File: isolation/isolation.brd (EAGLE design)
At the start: 74.5 x 72.7 mm, 81 parts, among them IC1 XTLV61048DBVR, IC2 SN74HC14DRG3, IC3 SN74HCS32PWR, IC4 SN74HCS08DYYR, IC5 FDN359BN, IC6 FDN359BN, IC7 FDN359BN, IC8 FDN359BN, J1 S4B-PH-K-S(LF)(SN), J2 S4B-PH-K-S(LF)(SN), J3 S4B-PH-K-S(LF)(SN), J4 S4B-PH-K-S(LF)(SN), J5 S4B-PH-K-S(LF)(SN)

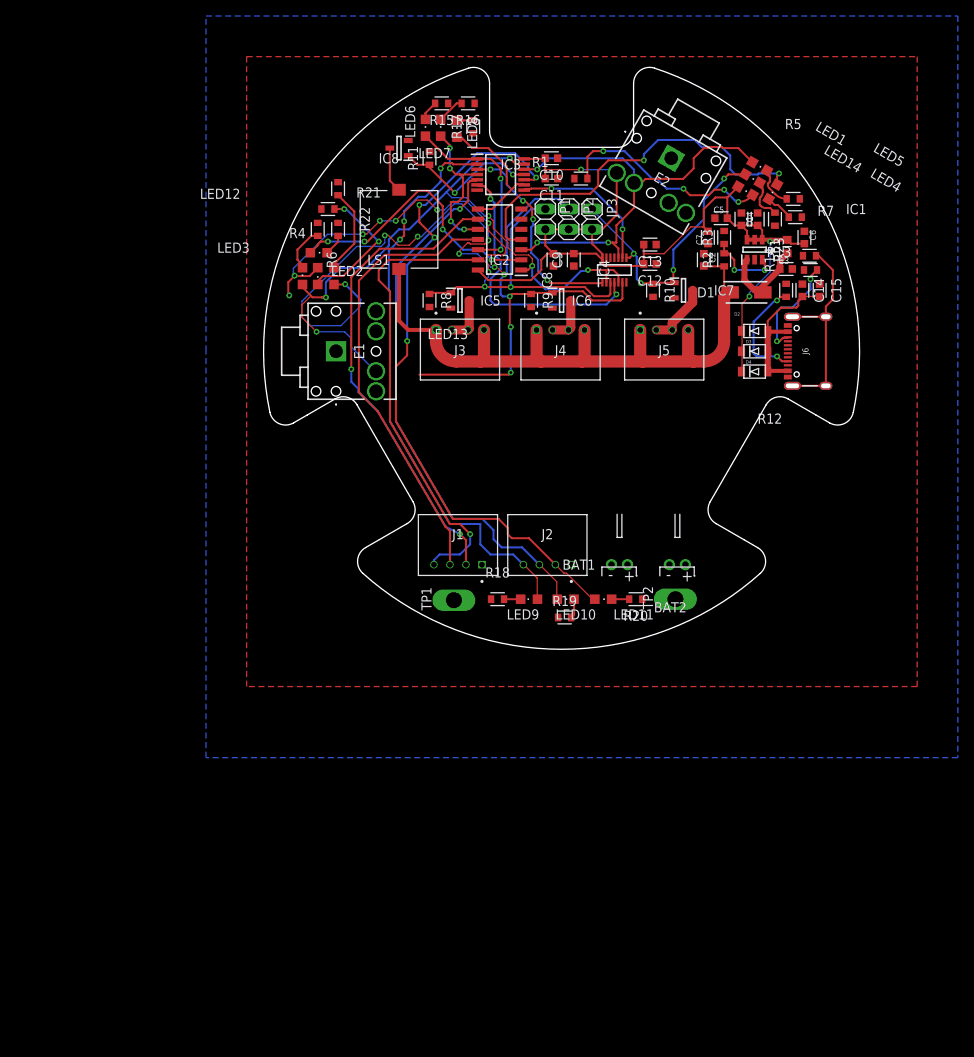
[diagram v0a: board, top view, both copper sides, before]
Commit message: 10mil dim line
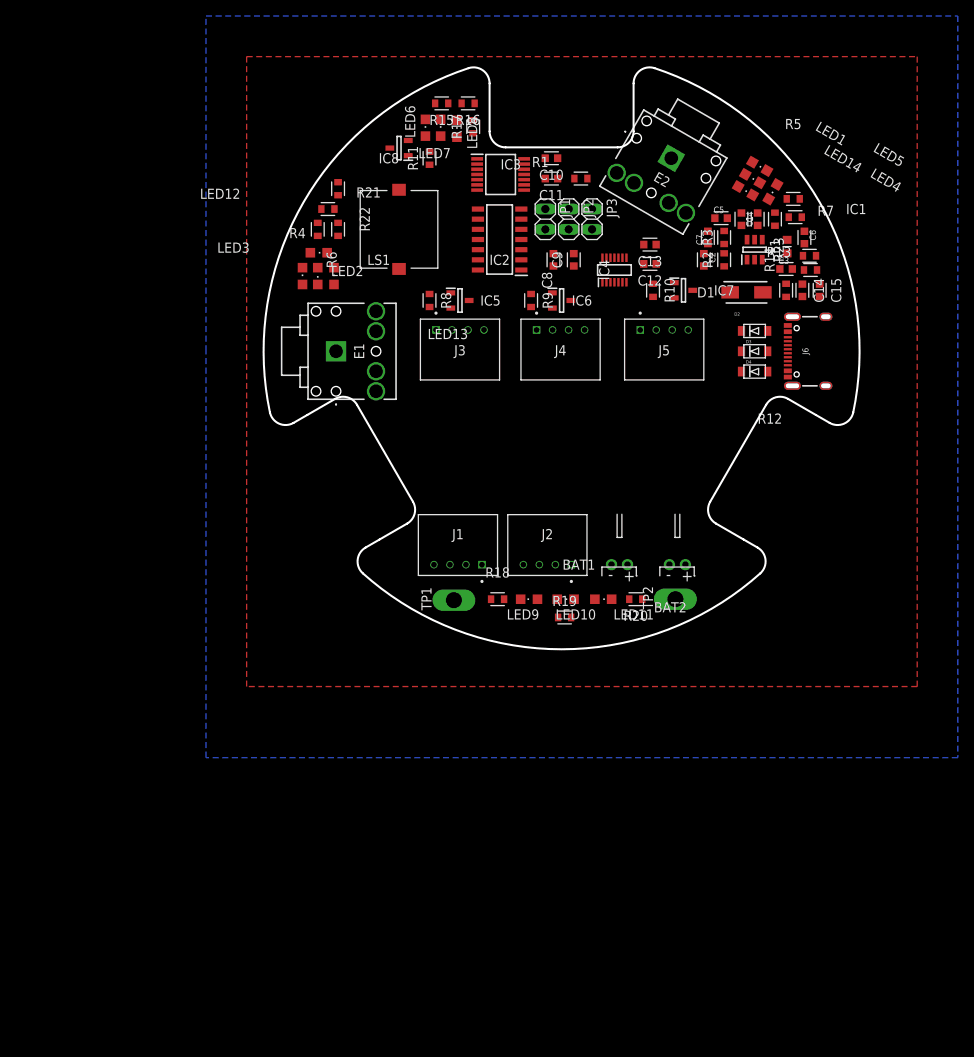
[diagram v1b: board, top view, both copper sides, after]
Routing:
- net VBAT: track 117.6 -> 0.00 mm, vias 3 -> 0
- net FIRE2: track 117.4 -> 0.00 mm, vias 10 -> 0
- net EN1: track 87.8 -> 0.00 mm, vias 6 -> 0
- net PICKLE3: track 86.7 -> 0.00 mm, vias 4 -> 0
- net FIRE1: track 86.2 -> 0.00 mm, vias 10 -> 0
- net VDEP: track 84.6 -> 0.00 mm
- net PICKLE1: track 72.8 -> 0.00 mm, vias 3 -> 0
- net PICKLE2: track 68.5 -> 0.00 mm, vias 1 -> 0
- net RAVEN3: track 59.9 -> 0.00 mm, vias 2 -> 0
- net EN2: track 57.7 -> 0.00 mm, vias 3 -> 0
- net RAVEN1: track 57.5 -> 0.00 mm, vias 1 -> 0
- net RAVEN2: track 56.1 -> 0.00 mm
- net SAFE2: track 49.2 -> 0.00 mm, vias 2 -> 0
- net FIRE3: track 36.1 -> 0.00 mm, vias 4 -> 0
- net SAFE1: track 34.9 -> 0.00 mm, vias 4 -> 0
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
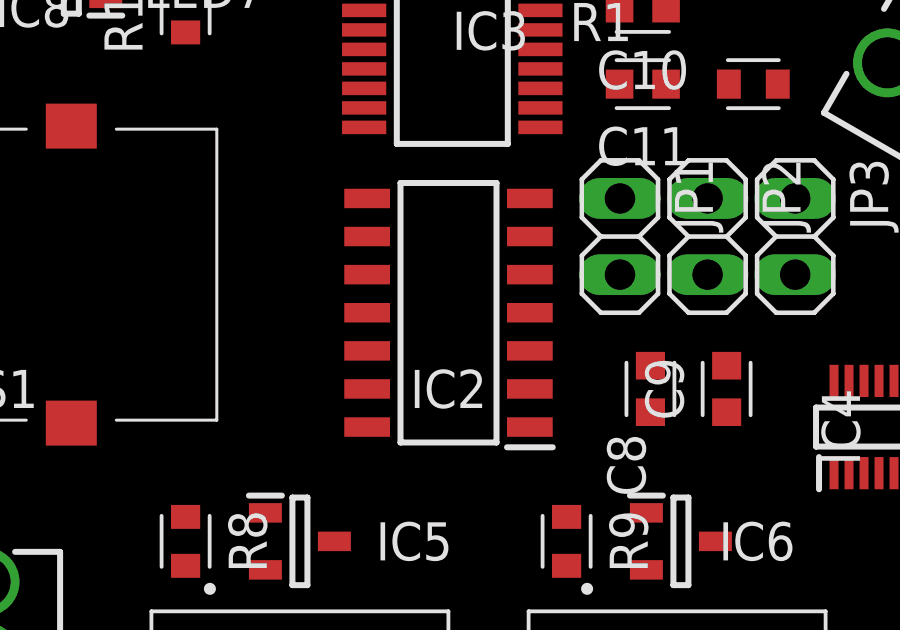
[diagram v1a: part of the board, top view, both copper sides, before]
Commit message: move to smaller inverter
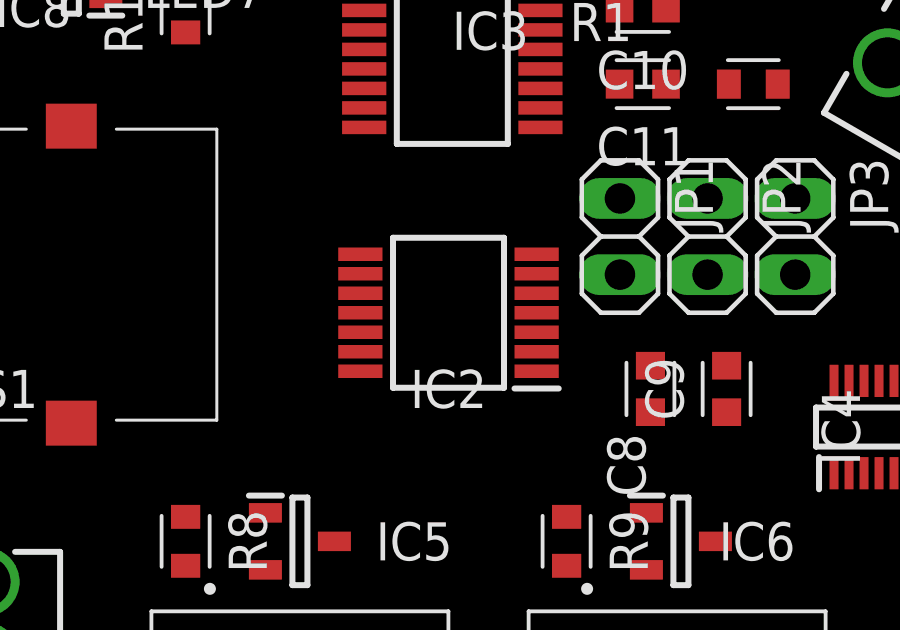
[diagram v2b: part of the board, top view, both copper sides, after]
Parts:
- IC2: value SN74HC14DRG3 -> SN74HC14PWR; device SamacSys_Parts:SOIC127P600X175-14N -> SamacSys_Parts:SOP65P640X120-14N
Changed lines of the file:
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@@
 <attribute name="VALUE" x="-27.844" y="0" size="1.27" layer="27" rot="R90" align="center"/>
 </element>
-<element name="IC2" library="SamacSys_Parts" package="SOIC127P600X175-14N" value="SN74HC14DRG3" x="-7.747" y="13.97" smashed="yes" rot="R180">
-<attribute name="ARROW_PART_NUMBER" value="SN74HC14DRG3" x="-7.747" y="13.97" size="1.778" layer="27" rot="R180" display="off"/>
-<attribute name="ARROW_PRICE-STOCK" value="https://www.arrow.com/en/products/sn74hc14drg3/texas-instruments?region=nac" x="-7.747" y="13.97" size="1.778" layer="27" rot="R180" display="off"/>
+<element name="IC2" library="SamacSys_Parts" package="SOP65P640X120-14N" value="SN74HC14PWR" x="-7.747" y="13.97" smashed="yes" rot="R180">
+<attribute name="ARROW_PART_NUMBER" value="SN74HC14PWR" x="-7.747" y="13.97" size="1.778" layer="27" rot="R180" display="off"/>
+<attribute name="ARROW_PRICE-STOCK" value="https://www.arrow.com/en/products/sn74hc14pwr/texas-instruments?region=nac" x="-7.747" y="13.97" size="1.778" layer="27" rot="R180" display="off"/>
 <attribute name="DESCRIPTION" value="Hex Schmitt-Trigger Inverters" x="-7.747" y="13.97" size="1.778" layer="27" rot="R180" display="off"/>
-<attribute name="HEIGHT" value="1.75mm" x="-7.747" y="13.97" size="1.778" layer="27" rot="R180" display="off"/>
+<attribute name="HEIGHT" value="1.2mm" x="-7.747" y="13.97" size="1.778" layer="27" rot="R180" display="off"/>
 <attribute name="MANUFACTURER_NAME" value="Texas Instruments" x="-7.747" y="13.97" size="1.778" layer="27" rot="R180" display="off"/>
-<attribute name="MANUFACTURER_PART_NUMBER" value="SN74HC14DRG3" x="-7.747" y="13.97" size="1.778" layer="27" rot="R180" display="off"/>
-<attribute name="MOUSER_PART_NUMBER" value="595-SN74HC14DRG3" x="-7.747" y="13.97" size="1.778" layer="27" rot="R180" display="off"/>
-<attribute name="MOUSER_PRICE-STOCK" value="https://www.mouser.co.uk/ProductDetail/Texas-Instruments/SN74HC14DRG3?qs=EuM%2FBx4ov4QCZjgspzZGxg%3D%3D" x="-7.747" y="13.97" size="1.778" layer="27" rot="R180" display="off"/>
+<attribute name="MANUFACTURER_PART_NUMBER" value="SN74HC14PWR" x="-7.747" y="13.97" size="1.778" layer="27" rot="R180" display="off"/>
+<attribute name="MOUSER_PART_NUMBER" value="595-SN74HC14PWR" x="-7.747" y="13.97" size="1.778" layer="27" rot="R180" display="off"/>
+<attribute name="MOUSER_PRICE-STOCK" value="https://www.mouser.co.uk/ProductDetail/Texas-Instruments/SN74HC14PWR?qs=YEaxc5757jODQ8PDizZzPA%3D%3D" x="-7.747" y="13.97" size="1.778" layer="27" rot="R180" display="off"/>
 <attribute name="NAME" x="-7.747" y="11.43" size="1.27" layer="25" rot="R180" align="center"/>
 <attribute name="VALUE" x="-7.747" y="13.97" size="1.27" layer="27" rot="R180" align="center"/>
@@
 <wire x1="-1.15" y1="5.4" x2="-1.016" y2="10.6554" width="0" layer="19" extent="1-1"/>
 <wire x1="-3.81" y1="5.5348" x2="-1.15" y2="5.4" width="0" layer="19" extent="1-1"/>
+<wire x1="-4.809" y1="14.62" x2="-1.016" y2="10.6554" width="0" layer="19" extent="1-1"/>
+<wire x1="-4.809" y1="15.92" x2="-4.809" y2="14.62" width="0" layer="19" extent="1-1"/>
 <wire x1="13.716" y1="24.13" x2="13.3810625" y2="18.549871875" width="0" layer="19" extent="1-1"/>
-<wire x1="-5.035" y1="15.24" x2="-1.016" y2="10.6554" width="0" layer="19" extent="1-1"/>
-<wire x1="-5.035" y1="17.78" x2="-5.035" y2="15.24" width="0" layer="19" extent="1-1"/>
-<wire x1="-0.4954" y1="21.59" x2="-5.035" y2="17.78" width="0" layer="19" extent="1-1"/>
+<wire x1="28.28" y1="-3.225" x2="28.28" y2="3.225" width="0" layer="19" extent="1-1"/>
+<wire x1="-0.4954" y1="21.59" x2="-4.809" y2="15.92" width="0" layer="19" extent="1-1"/>
 <wire x1="1.5978" y1="21.59" x2="-0.4954" y2="21.59" width="0" layer="19" extent="1-1"/>
 <wire x1="-0.4954" y1="24.13" x2="-0.4954" y2="21.59" width="0" layer="19" extent="1-1"/>
-<wire x1="-10.558" y1="20.148" x2="-5.035" y2="17.78" width="0" layer="19" extent="1-1"/>
-<wire x1="28.28" y1="-3.225" x2="28.28" y2="3.225" width="0" layer="19" extent="1-1"/>
+<wire x1="-10.558" y1="20.148" x2="-4.809" y2="15.92" width="0" layer="19" extent="1-1"/>
 <wire x1="-11.049" y1="27.2518" x2="-10.558" y2="20.148" width="0" layer="19" extent="1-1"/>
 <wire x1="-10.8688" y1="30.988" x2="-11.049" y2="27.2518" width="0" layer="19" extent="1-1"/>
@@
 <wire x1="-4.682" y1="24.048" x2="-2.0446" y2="24.13" width="0" layer="19" extent="1-1"/>
 <wire x1="6.885871875" y1="22.299871875" x2="3.81" y2="15.24" width="0" layer="19" extent="1-1"/>
-<wire x1="-10.459" y1="10.16" x2="-1.016" y2="12.2046" width="0" layer="19" extent="1-1"/>
+<wire x1="-10.685" y1="12.02" x2="-2.032" y2="15.24" width="0" layer="19" extent="1-1"/>
 <wire x1="22.4925" y1="2.54" x2="23.18" y2="13.95" width="0" layer="19" extent="1-1"/>
 <wire x1="22.4925" y1="0" x2="22.4925" y2="2.54" width="0" layer="19" extent="1-1"/>
 <wire x1="22.4925" y1="-2.54" x2="22.4925" y2="0" width="0" layer="19" extent="1-1"/>
-<wire x1="-23.194" y1="-5" x2="-10.459" y2="10.16" width="0" layer="19" extent="1-1"/>
+<wire x1="-23.194" y1="-5" x2="-10.685" y2="12.02" width="0" layer="19" extent="1-1"/>
 <wire x1="15.478" y1="-26.67" x2="22.4925" y2="-2.54" width="0" layer="19" extent="1-1"/>
 <wire x1="14.224" y1="-30.988" x2="15.478" y2="-26.67" width="0" layer="19" extent="1-1"/>
@@
 <contactref element="IC3" pad="13"/>
 <wire x1="-23.194" y1="-2.5" x2="-32.385" y2="8.348" width="0" layer="19" extent="1-1"/>
-<wire x1="-5.035" y1="10.16" x2="-23.194" y2="-2.5" width="0" layer="19" extent="1-1"/>
-<wire x1="5.604" y1="8.622" x2="-5.035" y2="10.16" width="0" layer="19" extent="1-1"/>
+<wire x1="-4.809" y1="12.02" x2="-23.194" y2="-2.5" width="0" layer="19" extent="1-1"/>
+<wire x1="5.604" y1="8.622" x2="-4.809" y2="12.02" width="0" layer="19" extent="1-1"/>
 <wire x1="7.104" y1="8.622" x2="5.604" y2="8.622" width="0" layer="19" extent="1-1"/>
-<wire x1="-4.682" y1="23.398" x2="-5.035" y2="10.16" width="0" layer="19" extent="1-1"/>
+<wire x1="-4.682" y1="23.398" x2="-4.809" y2="12.02" width="0" layer="19" extent="1-1"/>
 </signal>
 <signal name="N$5">
@@
 <contactref element="IC2" pad="2"/>
 <contactref element="LED3" pad="A"/>
-<wire x1="-5.035" y1="11.43" x2="-31.403" y2="12.319" width="0" layer="19" extent="1-1"/>
+<wire x1="-4.809" y1="12.67" x2="-31.403" y2="12.319" width="0" layer="19" extent="1-1"/>
 </signal>
 <signal name="EN2">
@@
 <wire x1="9.050934375" y1="21.049871875" x2="23.855671875" y2="23.639" width="0" layer="19" extent="1-1"/>
 <wire x1="7.104" y1="11.698" x2="9.050934375" y2="21.049871875" width="0" layer="19" extent="1-1"/>
-<wire x1="-5.035" y1="12.7" x2="7.104" y2="11.698" width="0" layer="19" extent="1-1"/>
-<wire x1="-4.682" y1="22.748" x2="-5.035" y2="12.7" width="0" layer="19" extent="1-1"/>
+<wire x1="-4.809" y1="13.32" x2="7.104" y2="11.698" width="0" layer="19" extent="1-1"/>
+<wire x1="-4.682" y1="22.748" x2="-4.809" y2="13.32" width="0" layer="19" extent="1-1"/>
 </signal>
 <signal name="SAFE2">
 <contactref element="IC2" pad="4"/>
 <contactref element="LED5" pad="A"/>
-<wire x1="-5.035" y1="13.97" x2="26.941" y2="20.848325" width="0" layer="19" extent="1-1"/>
+<wire x1="-4.809" y1="13.97" x2="26.941" y2="20.848325" width="0" layer="19" extent="1-1"/>
 </signal>
 <signal name="N$6">
@@
 <contactref element="J1" pad="2"/>
 <contactref element="IC2" pad="9"/>
-<wire x1="-10.459" y1="16.51" x2="-11.954" y2="-26.67" width="0" layer="19" extent="1-1"/>
+<wire x1="-10.685" y1="15.27" x2="-11.954" y2="-26.67" width="0" layer="19" extent="1-1"/>
 </signal>
 <signal name="RAVEN2">
 <contactref element="J1" pad="3"/>
 <contactref element="IC2" pad="11"/>
-<wire x1="-10.459" y1="13.97" x2="-13.954" y2="-26.67" width="0" layer="19" extent="1-1"/>
+<wire x1="-10.685" y1="13.97" x2="-13.954" y2="-26.67" width="0" layer="19" extent="1-1"/>
 </signal>
 <signal name="RAVEN1">
 <contactref element="J1" pad="4"/>
 <contactref element="IC2" pad="13"/>
-<wire x1="-10.459" y1="11.43" x2="-15.954" y2="-26.67" width="0" layer="19" extent="1-1"/>
+<wire x1="-10.685" y1="12.67" x2="-15.954" y2="-26.67" width="0" layer="19" extent="1-1"/>
 </signal>
 <signal name="FIRE1">
@@
 <contactref element="LED6" pad="A"/>
 <wire x1="-17.018" y1="26.89" x2="-10.558" y2="24.048" width="0" layer="19" extent="1-1"/>
-<wire x1="-10.459" y1="12.7" x2="-10.558" y2="24.048" width="0" layer="19" extent="1-1"/>
+<wire x1="-10.685" y1="13.32" x2="-10.558" y2="24.048" width="0" layer="19" extent="1-1"/>
 </signal>
 <signal name="INVR2">
@@
 <contactref element="LED7" pad="A"/>
 <wire x1="-10.558" y1="22.098" x2="-15.113" y2="26.89" width="0" layer="19" extent="1-1"/>
-<wire x1="-10.459" y1="15.24" x2="-10.558" y2="22.098" width="0" layer="19" extent="1-1"/>
+<wire x1="-10.685" y1="14.62" x2="-10.558" y2="22.098" width="0" layer="19" extent="1-1"/>
 </signal>
 <signal name="INVR3">
@@
 <contactref element="IC3" pad="9"/>
 <contactref element="LED8" pad="A"/>
-<wire x1="-10.459" y1="17.78" x2="-4.682" y2="20.798" width="0" layer="19" extent="1-1"/>
-<wire x1="-13.081" y1="26.763" x2="-10.459" y2="17.78" width="0" layer="19" extent="1-1"/>
+<wire x1="-10.685" y1="15.92" x2="-4.682" y2="20.798" width="0" layer="19" extent="1-1"/>
+<wire x1="-13.081" y1="26.763" x2="-4.682" y2="20.798" width="0" layer="19" extent="1-1"/>
 </signal>
 <signal name="COM1">

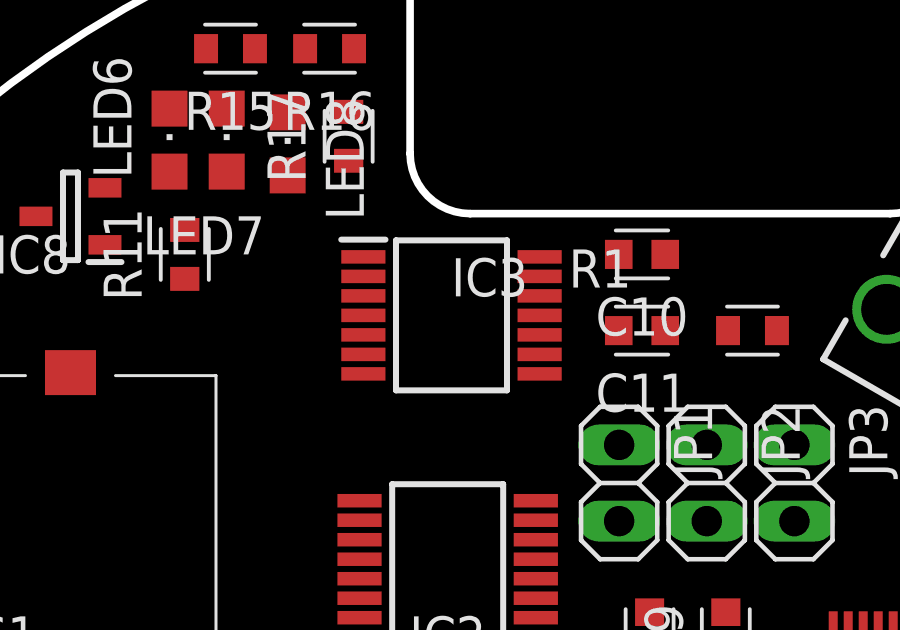
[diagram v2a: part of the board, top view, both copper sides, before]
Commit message: smaller OR IC
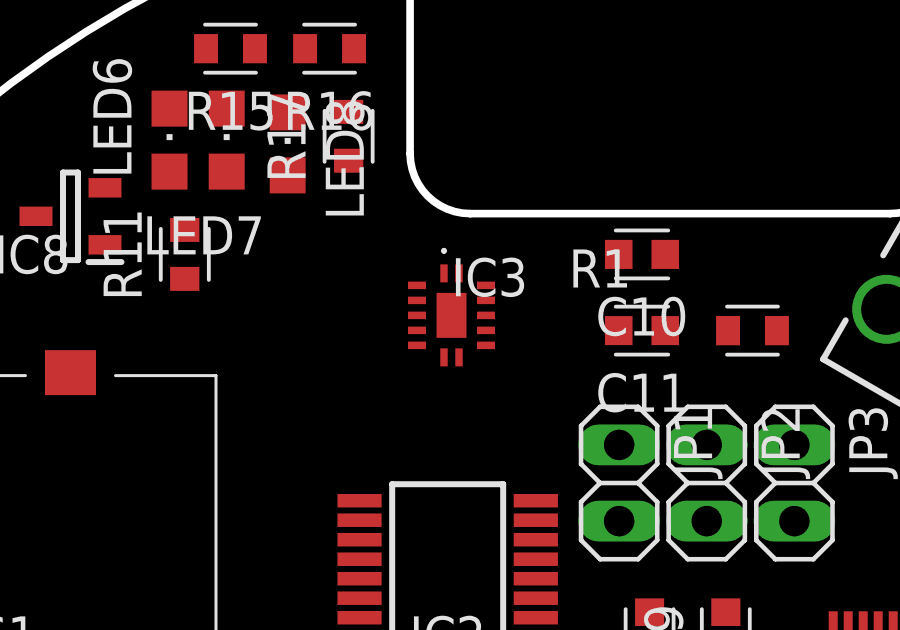
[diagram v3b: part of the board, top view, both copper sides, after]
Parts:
- IC3: value SN74HCS32PWR -> SN74HCS32BQAR; device SamacSys_Parts:SOP65P640X120-14N -> SamacSys_Parts:SN74HCS32BQAR
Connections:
- net EN1: now also IC3.12; no longer IC3.13
- net EN2: now also IC3.13; no longer IC3.12
- net GND: now also IC3.15
